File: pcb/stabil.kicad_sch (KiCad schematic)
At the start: 46 parts, among them Q10 IRFR5305, Q11 BT148, U11 TPS5430DDA, U12 LM75B, U13 INA219AxD, U14 LM78M05_TO252, U16 TSV911IDT, U17 PC817

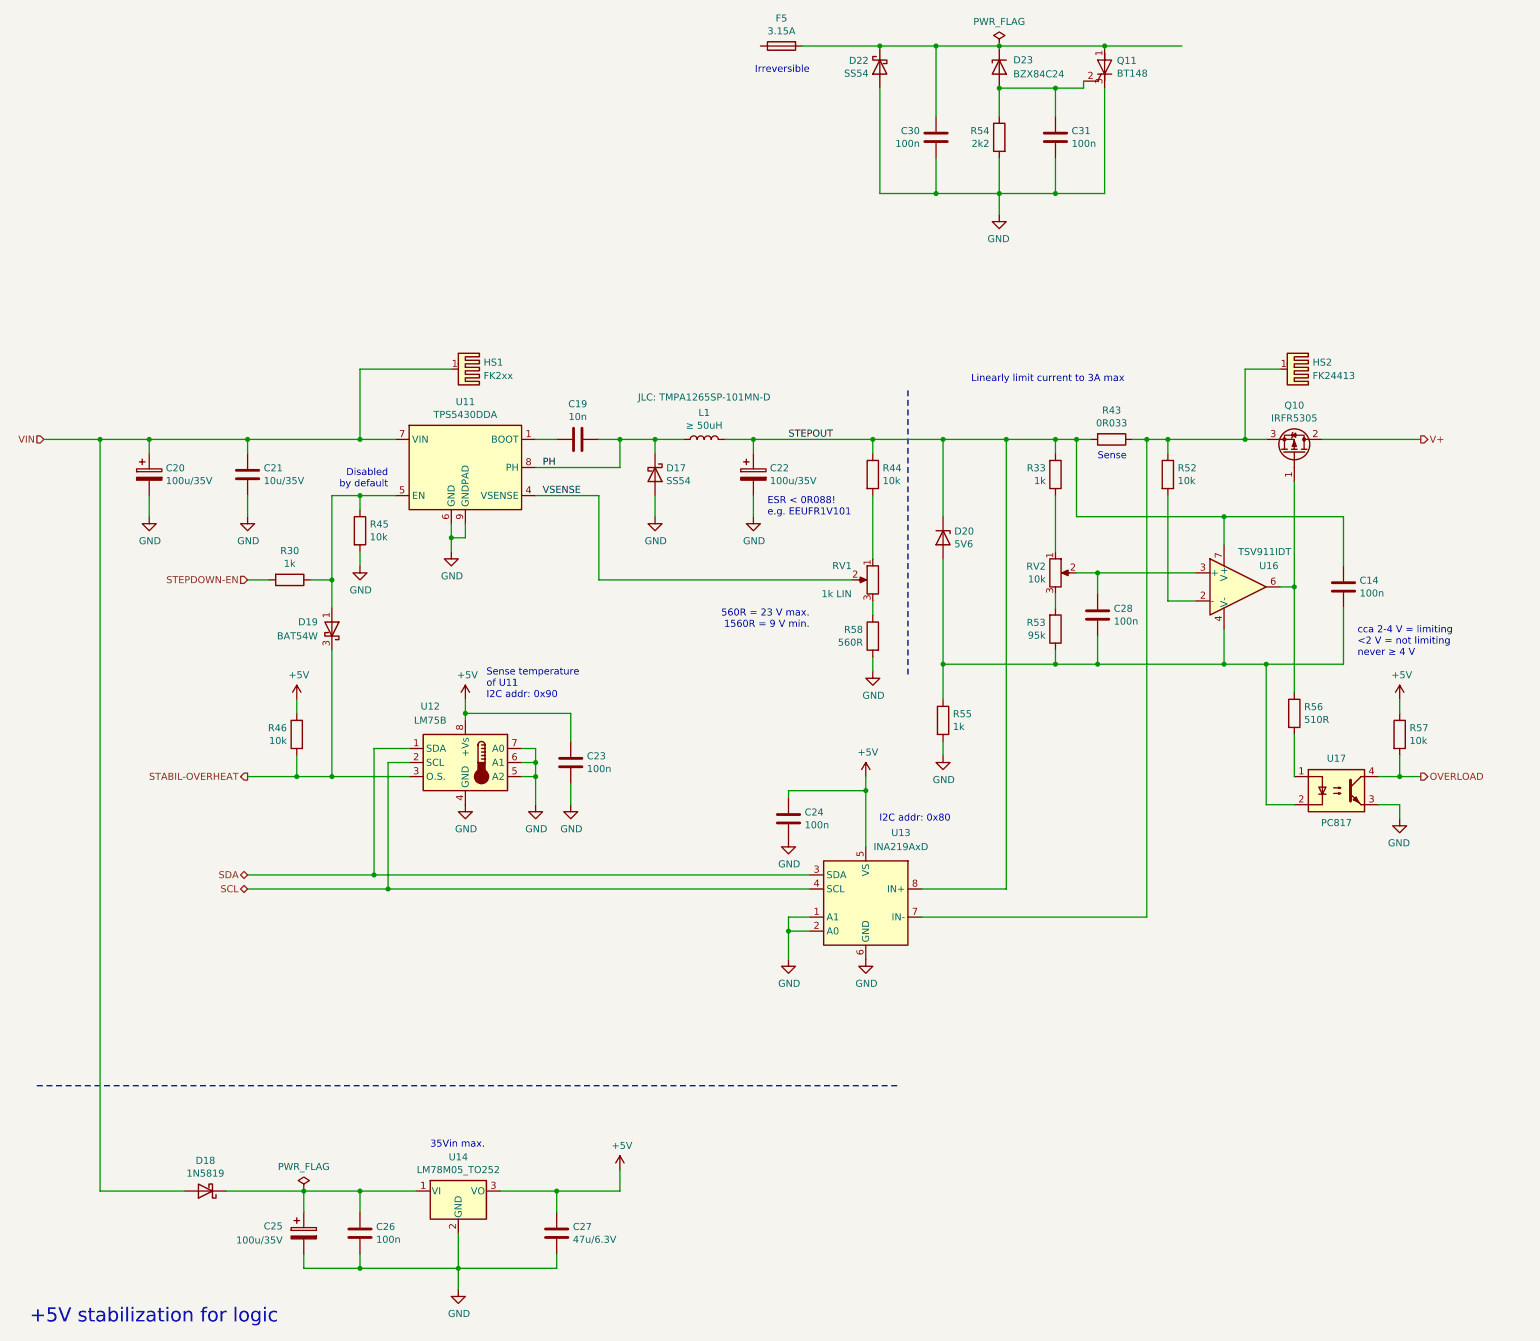
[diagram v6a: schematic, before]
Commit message: Add temp. sensor for current limiter.
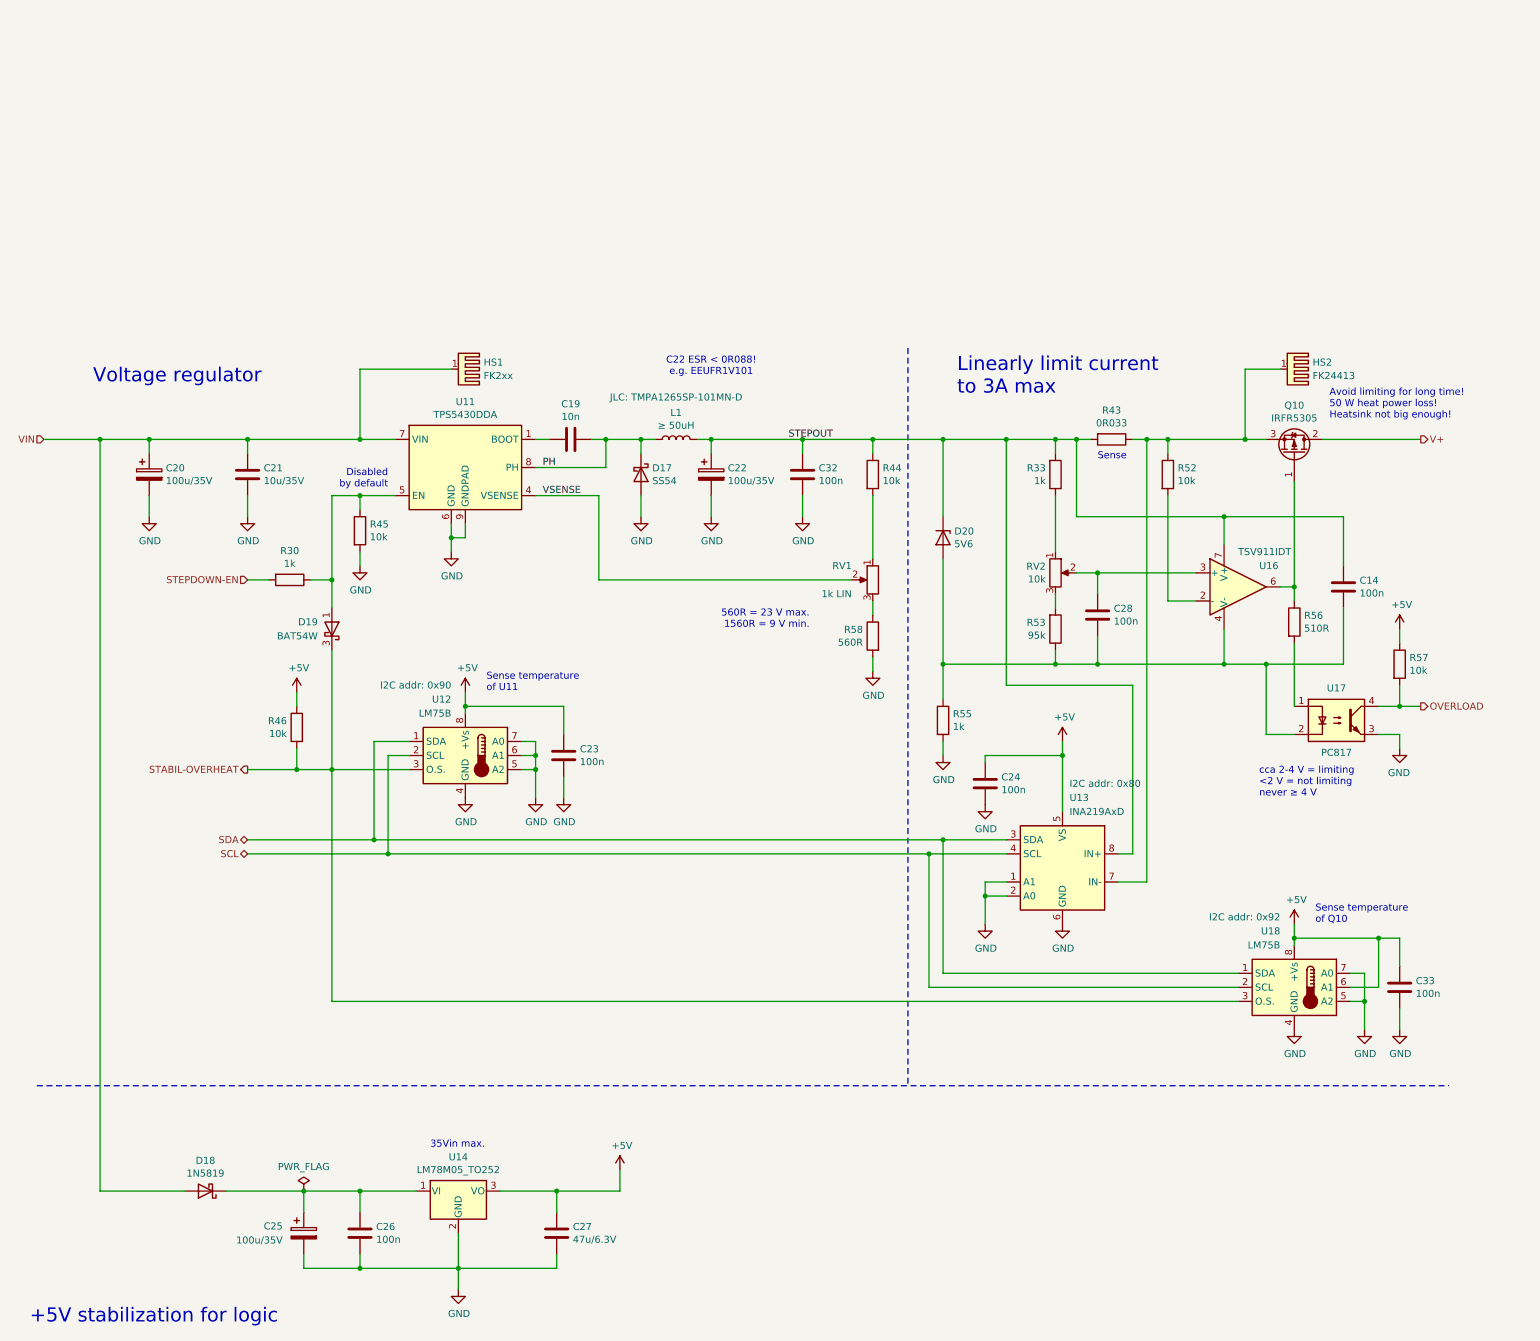
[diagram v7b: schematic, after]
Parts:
- removed C30, C31: 100n, Capacitor_SMD:C_0805_2012Metric, symbol Device:C
- removed D22: SS54, Diode_SMD:D_SMA, symbol Device:D_Schottky
- removed D23: BZX84C24, Package_TO_SOT_SMD:SOT-23, symbol Diode:BZX84Cxx
- removed F5: 3.15A, Fuse:Fuseholder_Cylinder-5x20mm_Stelvio-Kontek_PTF78_Horizontal_Open, symbol Device:Fuse
- removed Q11: BT148, Package_TO_SOT_THT:TO-92_Inline, symbol Triac_Thyristor:BT169D
- removed R54: 2k2, Resistor_SMD:R_0805_2012Metric, symbol Device:R
- added C32, C33: 100n, Capacitor_SMD:C_0805_2012Metric, symbol Device:C
- added U18: LM75B, Package_SO:SOIC-8_3.9x4.9mm_P1.27mm, symbol Sensor_Temperature:LM75B
- U12: I2C addr (none) -> 0x90
- U13: I2C addr (none) -> 0x80
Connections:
- net +5V: now also C33.1, U18.6 (A1), U18.8 (+Vs)
- net GND: now also C32.2, C33.2, U18.4 (GND), U18.5 (A2), U18.7 (A0)
- net SCL: now also U18.2 (SCL)
- net SDA: now also U18.1 (SDA)
- net STABIL-OVERHEAT: now also U18.3 (O.S.)
- net STEPOUT: now also C32.1
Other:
- note added: "Avoid limiting for long time! 50 W heat power loss! Heatsink not big enough!"
- note added: "C22 ESR < 0R088! e.g. EEUFR1V101"
- note added: "Sense temperature of Q10"
- note added: "Sense temperature of U11"
- note added: "Voltage regulator"
- note removed: "ESR < 0R088! e.g. EEUFR1V101"
- note removed: "I2C addr: 0x80"
- note removed: "Irreversible"
- note removed: "Sense temperature of U11 I2C addr: 0x90"
- moved on the sheet: C19, C22, C23, C24, D17, L1, R46, R56, R57, U12, U13, U17

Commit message: Specify screw terminals, add footprints.
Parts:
- L1: footprint (none) -> Inductor_SMD:L_TaiTech_TMPC1265_13.5x12.5mm
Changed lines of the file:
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@@
 			)
 		)
-		(property "Footprint" ""
+		(property "Footprint" "Inductor_SMD:L_TaiTech_TMPC1265_13.5x12.5mm"
 			(at 135.89 30.48 0)
 			(effects
